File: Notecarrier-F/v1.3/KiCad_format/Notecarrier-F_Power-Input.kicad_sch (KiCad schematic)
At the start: 21 parts, among them J1 S2BPHSM4TBLFSN, J2 S2BPHSM4TBLFSN, J3 S2BPHSM4TBLFSN, J4 10118193-0001LF, U2 BQ24210DQCT

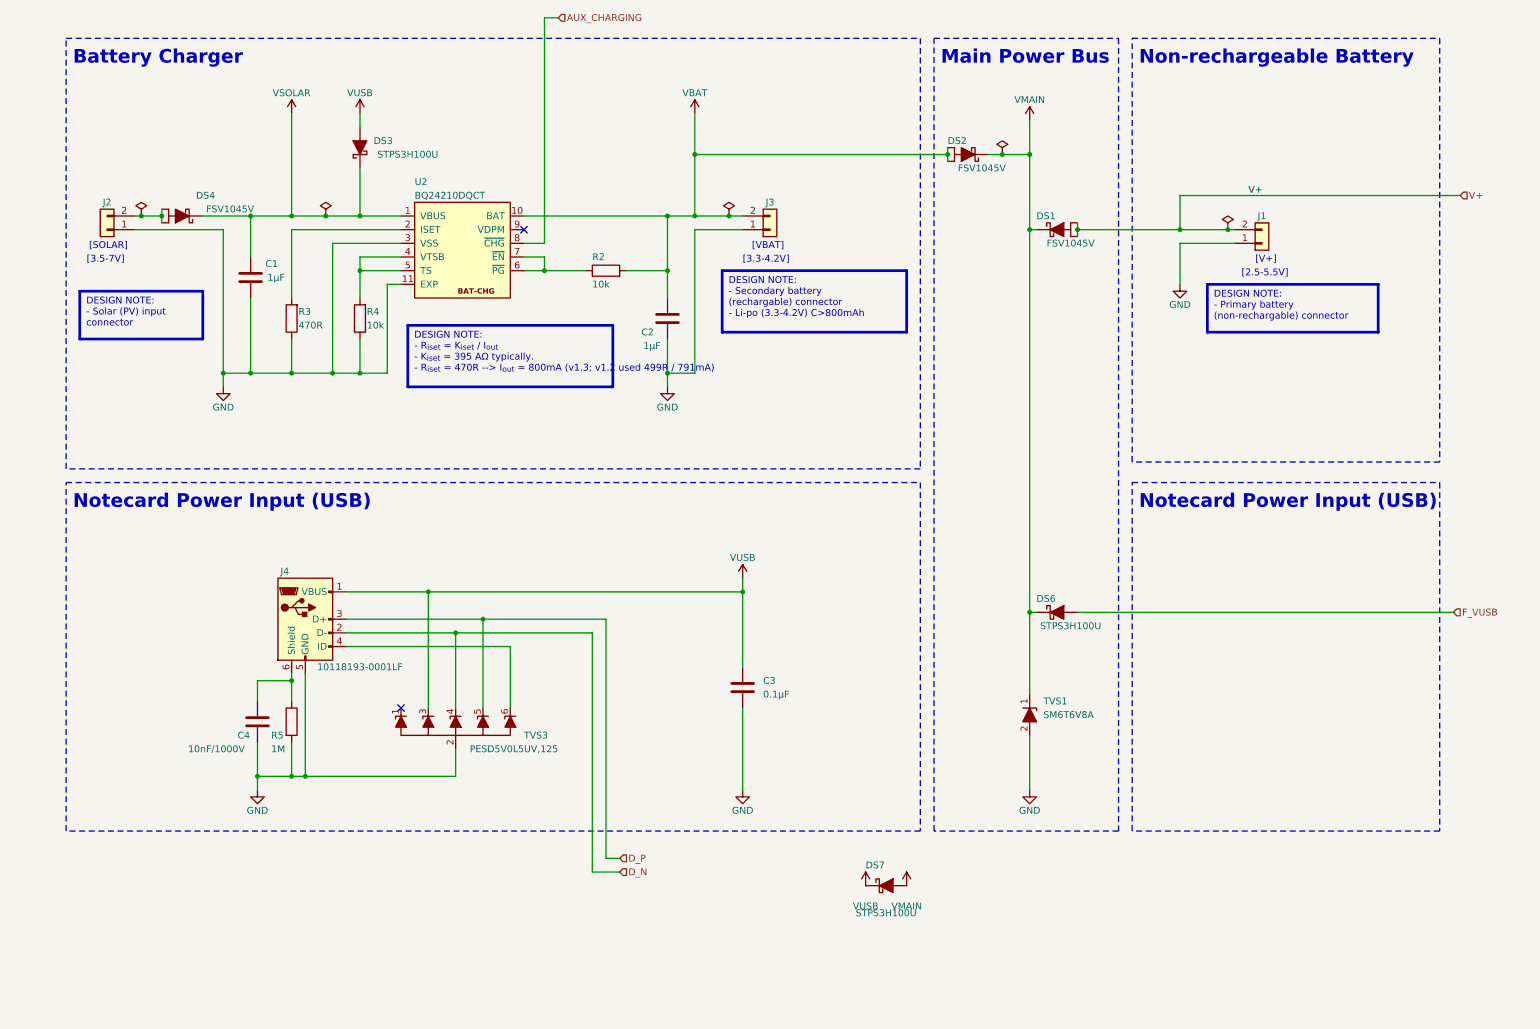
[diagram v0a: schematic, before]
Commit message: Notecarrier-F v1.3: KiCad 9 port from the release-day Altium sources
Replace the hand-made KiCad 7 port (which described v1.2, with a half-applied
v1.3 schematic delta and an ERRATA file) with a direct import of the v1.3
Altium project, recovered from the design archive's history: committed by the
design house on 2023-07-10, the day of the 2200-814 fabrication package, with a
Rev 11 schematic PDF byte-identical to the one published here. The Altium
sources are published alongside as Notecarrier-F/v1.3/Altium, as for v1.5.

The port follows the v1.5 procedure (KiCad 9.0.9 Altium project importer plus
scripted cleanup, scripts kept under documentation/scripts). All validation
gates pass: ERC 0, DRC 0 with schematic parity, BOM exact (94/94 vs
3000-653-002), placement 89/89 vs PNP-3000-653-002, gerber diff exact on outer
copper and masks with the reviewed inner-annulus/silk classes frozen as the
baseline, KiCanvas and RAG. The KiCad netlist was also matched pad by pad
against the nets carried by the Altium board file (0 conflicts).

J9/J10 are fitted per the released BOM (the 2023-08-31 re-save of the project
flips the variant to match); J11/R11/R12 are DNP. Design rules follow the
board's own Altium rule set (0.1 mm clearance). The old hand-port notes are
kept as History_Porting-Notes-hand-port.md because the harness README cites
them for the gerber-diff recipe; the RAG exclusion comment and the product
README are updated accordingly.

Co-Authored-By: Claude Fable 5.1 <noreply@anthropic.com>
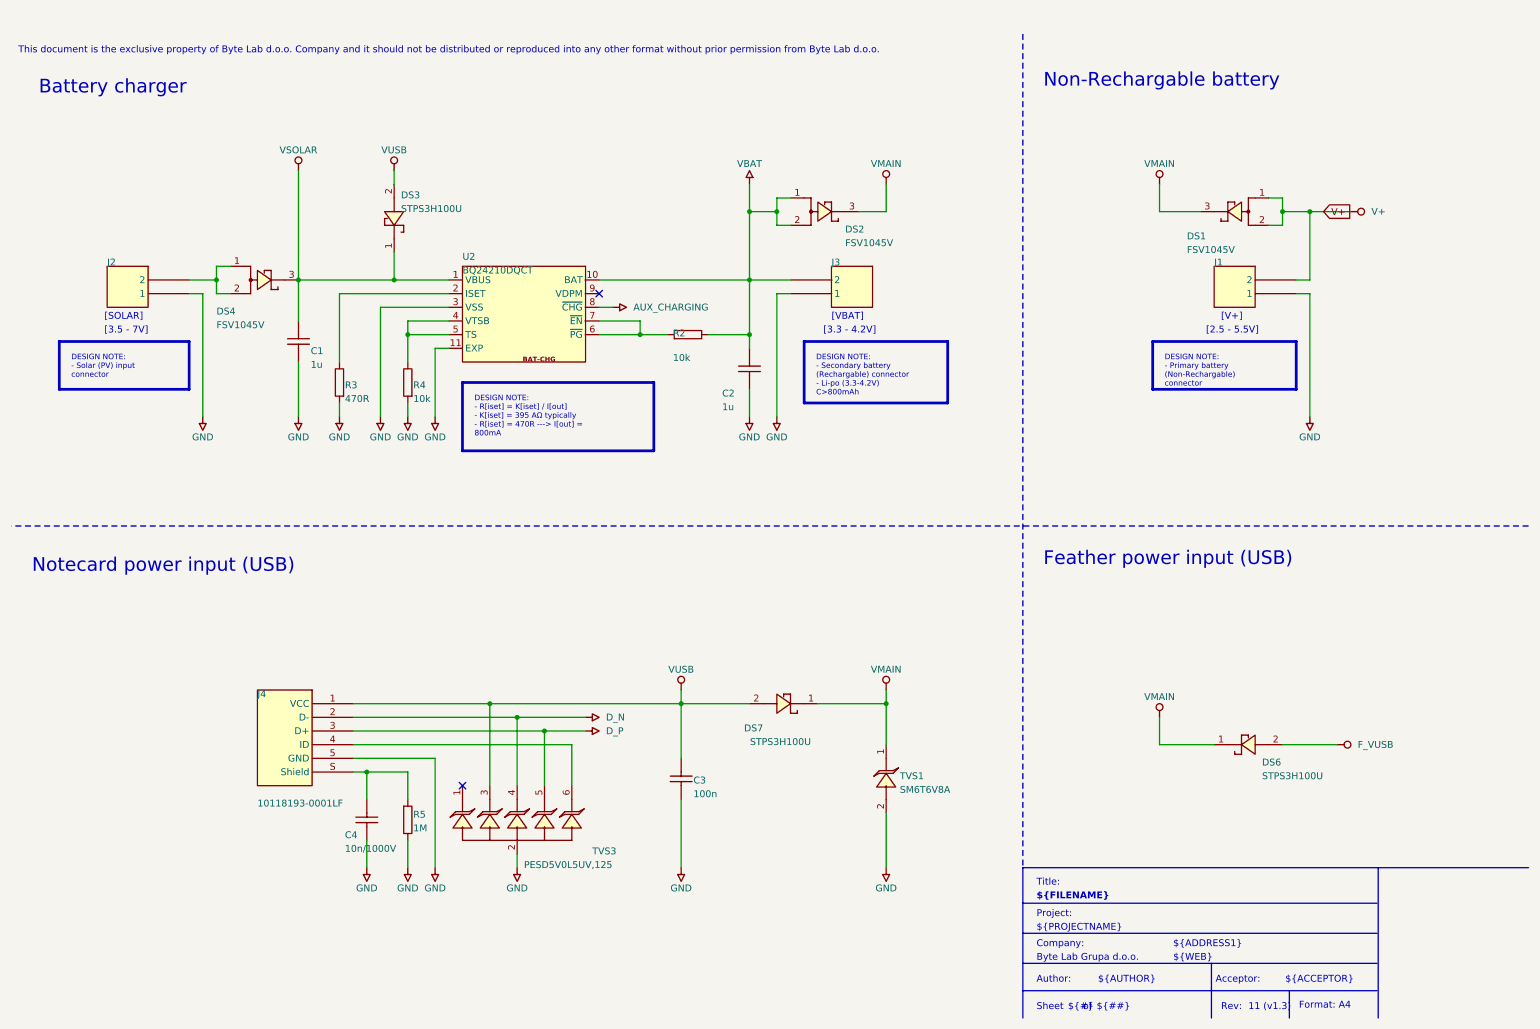
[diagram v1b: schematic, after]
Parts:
- removed C1, C2: 1µF, blues-kicad-lib:C-0603_Fv1.2, symbol Device:C
- removed C3: 0.1µF, blues-kicad-lib:C-0402_Fv1.2, symbol Device:C
- removed C4: 10nF/1000V, blues-kicad-lib:C-1206_Fv1.2, symbol Device:C
- removed DS1, DS2, DS4: FSV1045V, blues-kicad-lib:TO277-3, symbol blues-kicad-lib:FSV1045V
- removed DS3, DS6, DS7: STPS3H100U, blues-kicad-lib:SMB_Fv1.2, symbol blues-kicad-lib:D_Schottky_Filled_Swapped
- removed J1, J2, J3: S2BPHSM4TBLFSN, blues-kicad-lib:JST S2B-PH-SM4-TB_Fv1.2, symbol Connector_Generic:Conn_01x02
- removed J4: 10118193-0001LF, blues-kicad-lib:FCI USB 10118193-0001LF_Fv1.2, symbol Connector:USB_B_Micro
- removed R2, R4: 10k, blues-kicad-lib:R-0402_Fv1.2, symbol Device:R
- removed R3: 470R, blues-kicad-lib:R-0402_Fv1.2, symbol Device:R
- removed R5: 1M, blues-kicad-lib:R-1206_Fv1.2, symbol Device:R
- removed TVS1: SM6T6V8A, blues-kicad-lib:SMB_Fv1.2, symbol blues-kicad-lib:SM6T6V8A
- removed TVS3: PESD5V0L5UV,125, blues-kicad-lib:SOT666_Fv1.2, symbol blues-kicad-lib:PESD5V0L5UV
- removed U2: BQ24210DQCT, blues-kicad-lib:WSON10-EXP_Fv1.2, symbol blues-kicad-lib:BQ24210DQCT
- added C1: 1u, Notecarrier-F-altium-import:C-0603, symbol BL_Passive:root_1_mirrored_C0603-1u-25V-X5R_BL_Passive.SchLib
- added C2: 1u, Notecarrier-F-altium-import:C-0603, symbol BL_Passive:root_1_C0603-1u-25V-X5R_BL_Passive.SchLib
- added C3: 100n, Notecarrier-F-altium-import:C-0402, symbol BL_Passive:root_3_C0402-100n-16V-X7R_BL_Passive.SchLib
- added C4: 10n/1000V, Notecarrier-F-altium-import:C-1206, symbol BL_Passive:root_3_C1206-10n-1000V-X7R - CS1206KKX7RCBB103_BL_Passive.SchLib
- added DS1: FSV1045V, Notecarrier-F-altium-import:TO277-3, symbol n21-p2:root_0_mirrored_SCHOTTKY - FSV1045V - 10A/45V_n21-p2.SchLib
- added DS2, DS4: FSV1045V, Notecarrier-F-altium-import:TO277-3, symbol n21-p2:root_0_SCHOTTKY - FSV1045V - 10A/45V_n21-p2.SchLib
- added DS3: STPS3H100U, Notecarrier-F-altium-import:SMB, symbol n21-p2:root_1_SCHOTTKY-STPS3H100U - 3A/100V_n21-p2.SchLib
- added DS6: STPS3H100U, Notecarrier-F-altium-import:SMB, symbol n21-p2:root_0_SCHOTTKY-STPS3H100U - 3A/100V_n21-p2.SchLib
- added DS7: STPS3H100U, Notecarrier-F-altium-import:SMB, symbol n21-p2:root_0_mirrored_SCHOTTKY-STPS3H100U - 3A/100V_n21-p2.SchLib
- added J1, J2: S2BPHSM4TBLFSN, Notecarrier-F-altium-import:JST S2B-PH-SM4-TB, symbol n21-p2:root_2_mirrored_S2BPHSM4TBLFSN_n21-p2.SchLib
- added J3: S2BPHSM4TBLFSN, Notecarrier-F-altium-import:JST S2B-PH-SM4-TB, symbol n21-p2:root_2_S2BPHSM4TBLFSN_n21-p2.SchLib
- added J4: 10118193-0001LF, Notecarrier-F-altium-import:FCI USB 10118193-0001LF, symbol n21-p2:root_0_USB 2.0 Type B Micro_n21-p2.SchLib
- added R2: 10k, Notecarrier-F-altium-import:R-0402, symbol BL_Passive:root_0_R0402-10k-1_BL_Passive.SchLib
- added R3: 470R, Notecarrier-F-altium-import:R-0402, symbol BL_Passive:root_1_R0402-470R-1_BL_Passive.SchLib
- added R4: 10k, Notecarrier-F-altium-import:R-0402, symbol BL_Passive:root_1_R0402-10k-1_BL_Passive.SchLib
- added R5: 1M, Notecarrier-F-altium-import:R-1206, symbol BL_Passive:root_3_R1206-1M-1_BL_Passive.SchLib
- added TVS1: SM6T6V8A, Notecarrier-F-altium-import:SMB, symbol n21-p2:root_0_TVS-UNI - SM6T6V8A - 6.8V/600W_n21-p2.SchLib
- added TVS3: PESD5V0L5UV,125, Notecarrier-F-altium-import:SOT666, symbol n21-p2:root_0_PESD5V0L5UV,125_n21-p2.SchLib
- added U2: BQ24210DQCT, Notecarrier-F-altium-import:WSON10-EXP, symbol n21-p2:root_0_BAT-CHARGE - BQ24210DQCT_n21-p2.SchLib
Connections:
- net AUX_CHARGING: now also U2.8 (~{CHG})
- net D_N: now also J4.2 (D-), TVS3.4 (C4)
- net D_P: now also J4.3 (D+), TVS3.5 (A5)
- net F_VUSB: now also DS6.2 (A)
- net GND: now also C1.1, C2.1, C3.2, C4.2, J1.1, J2.1, J3.1, J4.5 (GND), R3.1, R4.1, R5.2, TVS1.2 (A), TVS3.2 (A2), U2.11 (EXP), U2.3 (VSS)
- net V+: now also DS1.1 (A1), DS1.2 (A2), J1.2
- net VBAT: now also C2.2, DS2.1 (A1), DS2.2 (A2), J3.2, R2.2, U2.10 (BAT)
- net VMAIN: now also DS1.3 (C), DS2.3 (C), DS6.1 (C), DS7.1 (C), TVS1.1 (C)
- net VSOLAR: now also C1.2, DS3.1 (C), DS4.3 (C), U2.1 (VBUS)
- net VUSB: now also C3.1, DS3.2 (A), DS7.2 (A), J4.1 (VCC), TVS3.3 (C3)
- new net: C4.1, J4.S (Shield), R5.1
- new net: J4.4 (ID), TVS3.6 (C6)
- new net: R3.2, U2.2 (ISET)
- new net: R2.1, U2.6 (~{PG}), U2.7 (~{EN})
- new net: R4.2, U2.4 (VTSB), U2.5 (TS)
- new net: DS4.1 (A1), DS4.2 (A2), J2.2
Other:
- note added: "${##}"
- note added: "${#}"
- note added: "${ACCEPTOR}"
- note added: "${ADDRESS1}"
- note added: "${AUTHOR}"
- note added: "${COMPANY}"
- note added: "${FILENAME}"
- note added: "${PROJECTNAME}"
- note added: "${REVISION}"
- note added: "${WEB}"
- note added: "Acceptor:"
- note added: "Author:"
- note added: "Battery charger"
- note added: "Company:"
- note added: "Feather power input (USB)"
- note added: "Format: A4"
- note added: "Non-Rechargable battery"
- note added: "Notecard power input (USB)"
- note added: "Project:"
- note added: "Rev:"
- note added: "Sheet"
- note added: "This document is the exclusive property of Byte Lab d.o.o. Company and it should not be distributed or reproduced into any other format without prior permission from Byte Lab d.o.o."
- note added: "Title:"
- note added: "[2.5 - 5.5V]"
- note added: "[3.3 - 4.2V]"
- note added: "[3.5 - 7V]"
- note added: "of"
- note removed: "Battery Charger"
- note removed: "DESIGN NOTE: - Primary battery (non-rechargable) connector"
- note removed: "DESIGN NOTE: - R_{iset} = K_{iset} / I_{out} - K_{iset} = 395 AΩ typically. - R_{iset} = 470R --> I_{out} = 800mA (v1.3; v1.2 used 499R / 791mA)"
- note removed: "DESIGN NOTE: - Secondary battery (rechargable) connector - Li-po (3.3-4.2V) C>800mAh"
- note removed: "DESIGN NOTE: - Solar (PV) input connector"
- note removed: "Main Power Bus"
- note removed: "Non-rechargeable Battery"
- note removed: "Notecard Power Input (USB)"
- note removed: "[2.5-5.5V]"
- note removed: "[3.3-4.2V]"
- note removed: "[3.5-7V]"
- company: (none) -> Byte Lab Grupa d.o.o.
